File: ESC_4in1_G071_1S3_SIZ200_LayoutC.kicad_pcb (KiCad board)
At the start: 4 copper layers, 26 x 27 mm, 176 parts, among them J1 Conn_01x08, U1 STM32G071GBU6, U10 NCP81161MNTBG, U11 SIZ200DT-T1-GE3, U12 NCP81161MNTBG, U13 SIZ200DT-T1-GE3, U14 TPS630701, U15 TPS72733DSE, U16 INA185, U17 STM32G071GBU6, U18 NCP81161MNTBG, U19 SIZ200DT-T1-GE3, U2 NCP81161MNTBG, U20 NCP81161MNTBG, U21 STM32G071GBU6, U22 SIZ200DT-T1-GE3, U23 NCP81161MNTBG, U24 SIZ200DT-T1-GE3, U25 NCP81161MNTBG, U26 SIZ200DT-T1-GE3, U27 NCP81161MNTBG, U28 STM32G071GBU6, U29 SIZ200DT-T1-GE3, U3 SIZ200DT-T1-GE3, U30 NCP81161MNTBG, U31 SIZ200DT-T1-GE3, U4 NCP81161MNTBG, U5 SIZ200DT-T1-GE3, U6 NCP81161MNTBG, U7 SIZ200DT-T1-GE3, U8 NCP81161MNTBG, U9 SIZ200DT-T1-GE3

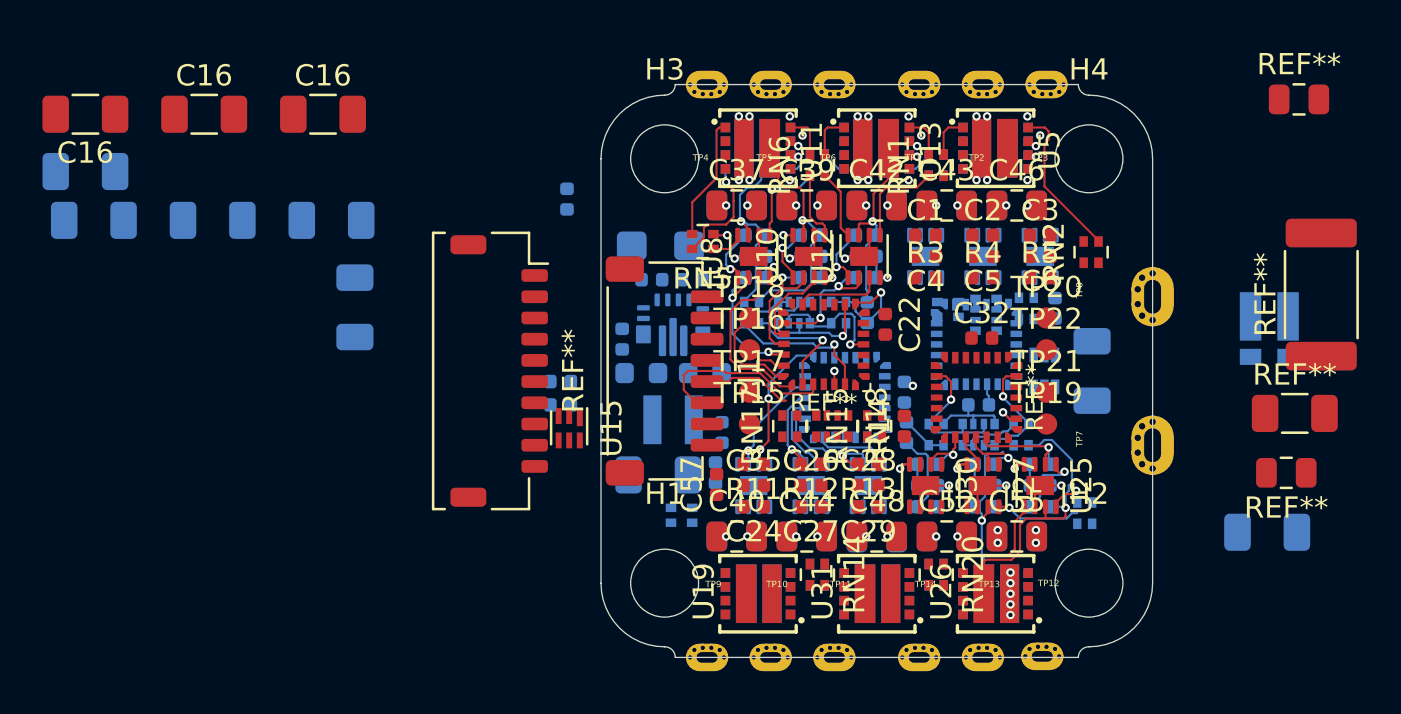
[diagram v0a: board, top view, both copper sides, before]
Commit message: update schematic and layout
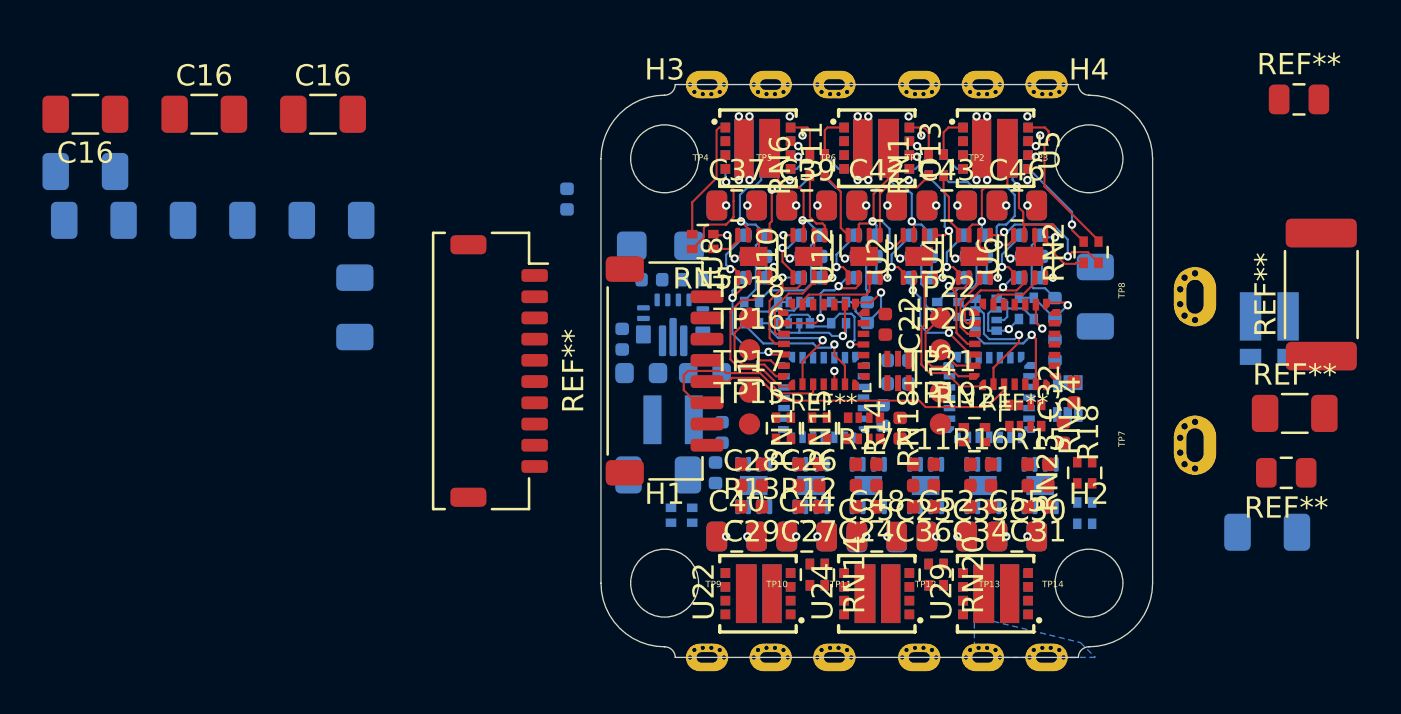
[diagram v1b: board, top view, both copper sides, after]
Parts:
- removed C57: 10u, Capacitor_SMD:C_0402_1005Metric
- C1, C2, C3, C4, C5, C6, R3, R4, R5, U19, U25, U26, U27, U28, U30, U31: moved to B.Cu
- C23, C30, C31, C33, C34, C36, R15, R16, R17, R18, RN21, RN23, RN24, U1, U2, U22, U24, U29, U4, U6: moved to F.Cu
- moved C18 15.9 mm to (137.0, 75.6)
- moved C19 15.9 mm to (137.0, 74.5)
- moved U15 15.7 mm to (137.0, 75.0)
- moved R11 8.00 mm to (138.2, 79.4), turned to 0 degrees
- moved R18 7.40 mm to (144.8, 77.9), turned to 270 degrees
- moved RN23 7.23 mm to (145.8, 79.8), turned to 90 degrees
- moved TP14 6.00 mm to (144.0, 88.5)
- moved TP12 5.80 mm to (138.0, 88.5)
- moved U26 5.60 mm to (136.0, 85.5), turned to 270 degrees
- moved U31 5.60 mm to (141.6, 85.5), turned to 270 degrees
- moved C28 5.50 mm to (130.1, 80.4)
- moved C29 5.50 mm to (130.1, 81.4)
- moved R13 5.50 mm to (130.1, 79.4)
- moved U18 5.40 mm to (135.6, 80.4)
- moved U23 5.40 mm to (130.2, 80.4)
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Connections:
- RN21 pad 1: /ESC3_A -> /ESC3_B
- RN21 pad 2: /ESC3_B -> /ESC3_A
- RN21 pad 3: /ESC3_MB -> /ESC3_MA
- RN21 pad 4: /ESC3_MA -> /ESC3_MB
- U21 pad 14: Net-(U21-Pad14) -> /ESC4_B_EN
- U21 pad 15: Net-(U21-Pad15) -> /ESC4_A_EN
- U21 pad 17: /ESC4_B_EN -> Net-(U21-Pad17)
- U21 pad 22: /ESC4_A_EN -> Net-(U21-Pad22)
- U28 pad 14: Net-(U28-Pad14) -> /ESC3_B_EN
- U28 pad 15: Net-(U28-Pad15) -> /ESC3_A_EN
- U28 pad 17: /ESC3_B_EN -> Net-(U28-Pad17)
- U28 pad 22: /ESC3_A_EN -> Net-(U28-Pad22)
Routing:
- net /ESC3_A: track 13.6 -> 0.00 mm, vias 1 -> 0
- net /ESC1_C: track 0.00 -> 11.4 mm, vias 0 -> 2
- net /ESC1_IN: track 4.32 -> 15.3 mm
- net /ESC1_B: track 0.00 -> 10.9 mm, vias 0 -> 1
- net /ESC1_A: track 0.00 -> 10.4 mm, vias 0 -> 1
- net /ESC3_B: track 8.59 -> 0.00 mm, vias 1 -> 0
- net /ESC1_C_DRVH: track 0.00 -> 7.85 mm, vias 0 -> 1
- net /ESC1_MB: track 0.00 -> 7.54 mm, vias 0 -> 1
- net /ESC1_A_EN: track 0.00 -> 7.49 mm
- net /ESC1_MA: track 0.00 -> 6.95 mm, vias 0 -> 1
- net /ESC3_Y: track 6.84 -> 0.00 mm, vias 1 -> 0
- net /ESC1_B_DRVL: track 0.00 -> 6.69 mm, vias 0 -> 2
- net /ESC4_A_EN: track 6.64 -> 0.00 mm, vias 2 -> 0
- net /ESC1_A_DRVH: track 0.00 -> 6.62 mm, vias 0 -> 1
- net /ESC1_A_PWM: track 0.00 -> 6.20 mm, vias 0 -> 2
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- added copper zone on B.Cu, net /ESC3_A
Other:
- board text removed: "LAYOUT C"
